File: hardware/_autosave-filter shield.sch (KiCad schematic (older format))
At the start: 23 parts, among them J1 Screw_Terminal_01x03, J2 Screw_Terminal_01x03, J3 TR switch Connector, J4 5V distribution, J5 12V distribution, J6 Screw_Terminal_01x03, J7 Radioberry Connector, J8 BPF Connector, J9 LPF Connector, Q1 PN2222A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

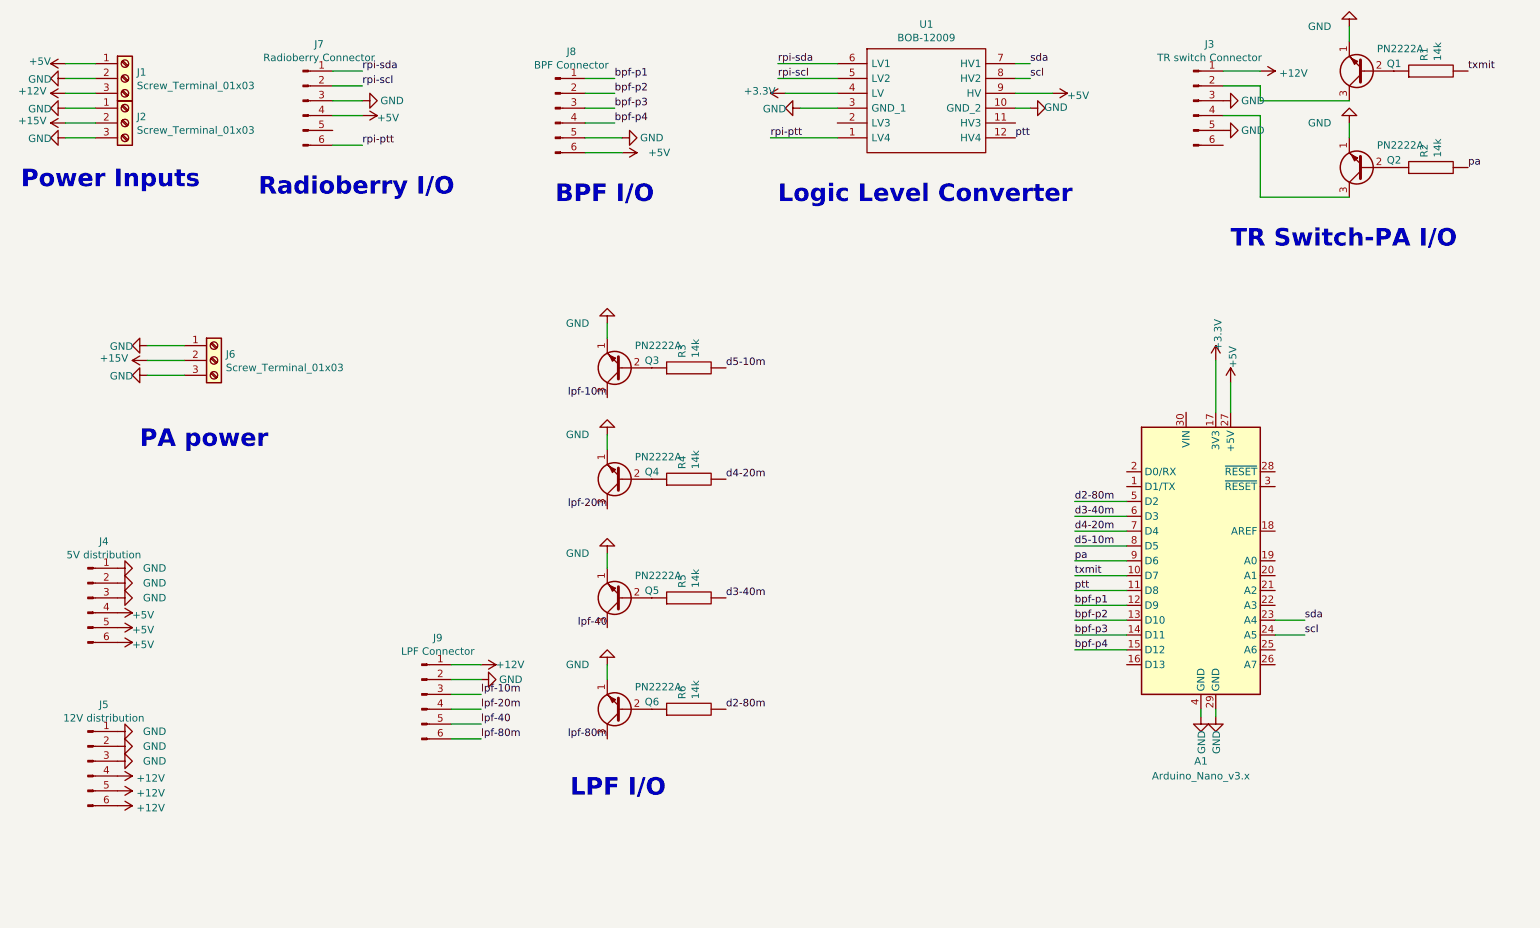
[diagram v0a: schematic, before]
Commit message: Revised circuit to meet lpf protocol. Added futur expansion i/o over analog pins
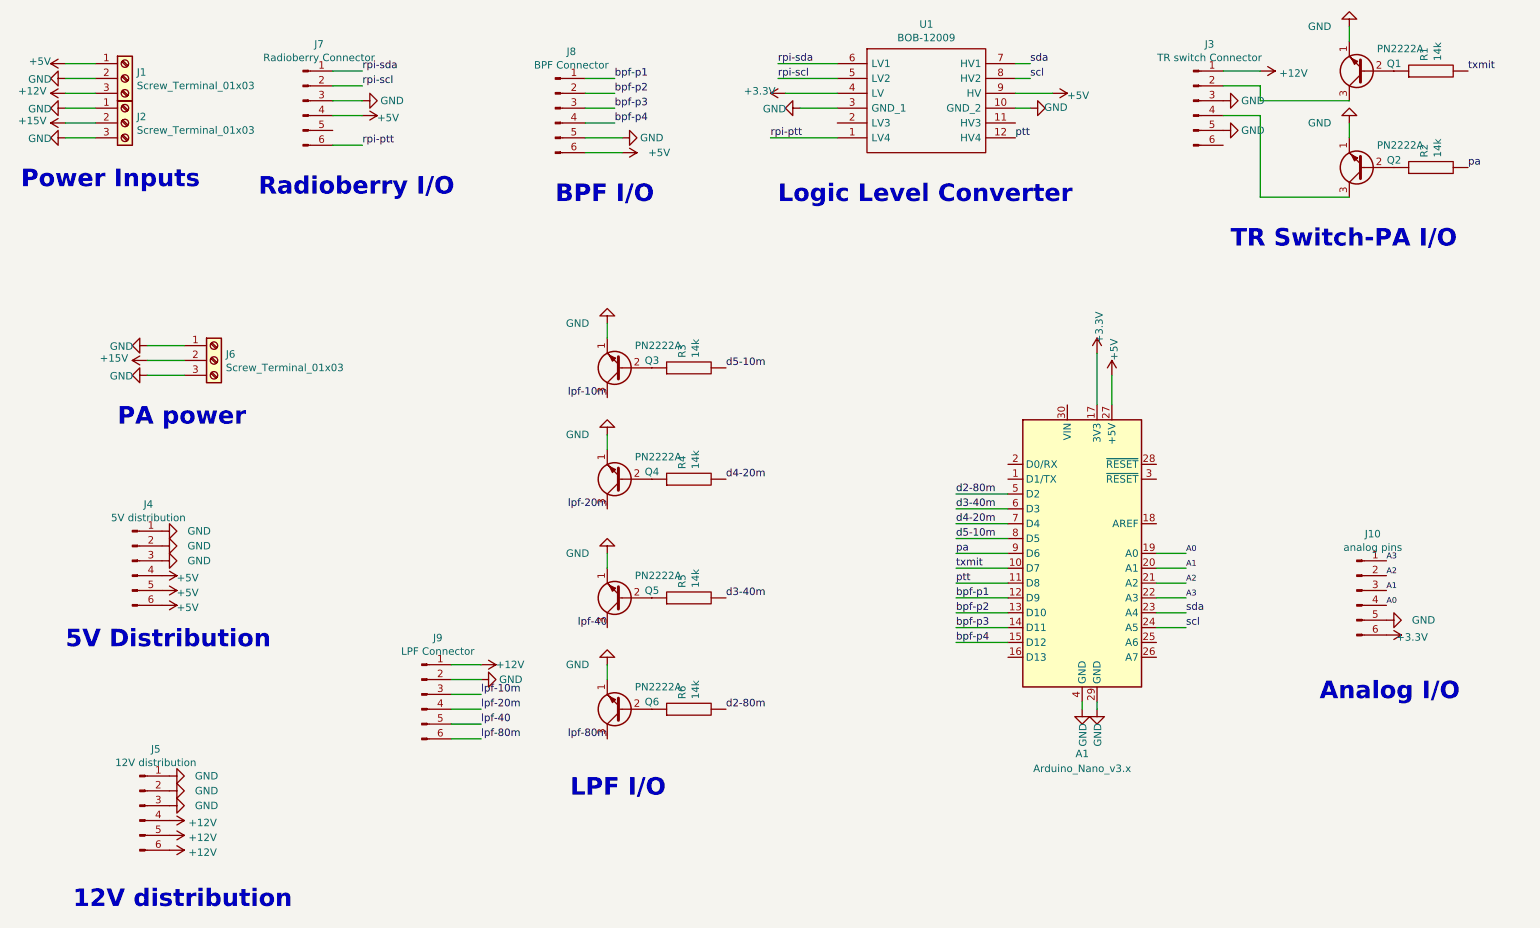
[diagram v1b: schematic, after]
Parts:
- added J10: analog pins, Connector_PinHeader_2.54mm:PinHeader_1x06_P2.54mm_Vertical, symbol Connector:Conn_01x06_Male
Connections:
- net +3V3: now also J10.6 (Pin_6)
- net GND: now also J10.5 (Pin_5)
- net A0: now reaches A1.19 (A0)
- net A0: now also J10.4 (Pin_4)
- net A1: now reaches A1.20 (A1)
- net A1: now also J10.3 (Pin_3)
- net A2: now reaches A1.21 (A2)
- net A2: now also J10.2 (Pin_2)
- net A3: now reaches A1.22 (A3)
- net A3: now also J10.1 (Pin_1)
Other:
- note added: "12V distribution"
- note added: "5V Distribution"
- note added: "Analog I/O"
- moved on the sheet: A1, J4, J5
